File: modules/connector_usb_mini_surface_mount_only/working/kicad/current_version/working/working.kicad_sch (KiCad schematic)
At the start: 1 part, among them J1 scumnsmo

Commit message: a few module workings
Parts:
- removed J1: scumnsmo, scumnsmo_electronic_socket_usb_mini_surface_mount_only, symbol oomlout_oomp_part_symbols:scumnsmo_electronic_socket_usb_mini_surface_mount_only
- added J3: scumnsmo, oomlout_oomp_part_kicad_footprints:scumnsmo_electronic_socket_usb_mini_surface_mount_only, symbol oomlout_oomp_part_symbols:scumnsmo_electronic_socket_usb_mini_surface_mount_only
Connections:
- net +5V: now also J3.1 (VBUS)
- net GND: now also J3.5 (GND), J3.6 (Shield)
- net usb_id: now also J3.4 (ID)
- net usb_negative: now also J3.2 (D-)
- net usb_plus: now also J3.3 (D+)
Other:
- note added: "name"
- note added: "usb_mini"
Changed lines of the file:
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@@
 (kicad_sch (version 20230121) (generator eeschema)
   (paper "A4")
-  (wire (pts (xy 175.26 69.85) (xy 172.72 69.85))
+  (junction (at 142.24 109.22) (diameter 0) (color 0 0 0 0)
+  )
+  (wire (pts (xy 149.86 96.52) (xy 152.4 96.52))
     (stroke (width 0) (type default))
   )
-  (wire (pts (xy 165.1 85.09) (xy 165.1 87.63))
+  (wire (pts (xy 142.24 106.68) (xy 142.24 109.22))
     (stroke (width 0) (type default))
   )
-  (wire (pts (xy 162.56 85.09) (xy 162.56 87.63))
+  (wire (pts (xy 152.4 91.44) (xy 149.86 91.44))
     (stroke (width 0) (type default))
   )
-  (wire (pts (xy 172.72 74.93) (xy 175.26 74.93))
+  (wire (pts (xy 139.7 106.68) (xy 139.7 109.22))
     (stroke (width 0) (type default))
   )
-  (wire (pts (xy 172.72 80.01) (xy 175.26 80.01))
+  (wire (pts (xy 149.86 99.06) (xy 152.4 99.06))
     (stroke (width 0) (type default))
   )
-  (wire (pts (xy 175.26 67.31) (xy 175.26 69.85))
+  (wire (pts (xy 139.7 109.22) (xy 142.24 109.22))
     (stroke (width 0) (type default))
   )
-  (wire (pts (xy 172.72 77.47) (xy 175.26 77.47))
+  (wire (pts (xy 149.86 101.6) (xy 152.4 101.6))
     (stroke (width 0) (type default))
   )
-  (rectangle (start 137.16 40.64) (end 200.66 105.41)
+  (wire (pts (xy 152.4 88.9) (xy 152.4 91.44))
+    (stroke (width 0) (type default))
+  )
+  (rectangle (start 139.7 62.23) (end 177.8 68.58)
+    (stroke (width 1) (type default))
+    (fill (type color) (color 0 0 0 0))
+  )
+  (rectangle (start 114.3 62.23) (end 177.8 127)
     (stroke (width 1) (type default))
     (fill (type none))
   )
-  (rectangle (start 199.39 97.79) (end 199.39 97.79)
-    (stroke (width 0) (type default))
-    (fill (type none))
-  )
-  (text "module\nconnector\nusb_mini\nsurface_mount_only\n\n" (at 138.43 60.96 0)
+  (text "module\nconnector\nusb_mini\nsurface_mount_only\n\n" (at 115.57 82.55 0)
     (effects (font (size 2.5 2.5)) (justify left bottom))
   )
-  (label "usb_id" (at 175.26 80.01 0) (fields_autoplaced)
+  (text "name" (at 142.24 68.58 90)
+    (effects (font (size 1.27 1.27) (thickness 0.254) bold (color 255 255 255 1)) (justify left bottom))
+  )
+  (text "usb_mini\n" (at 176.53 68.58 0)
+    (effects (font (size 4 4) (thickness 0.8) bold (color 255 255 255 1)) (justify right bottom))
+  )
+  (label "usb_negative" (at 152.4 99.06 0) (fields_autoplaced)
     (effects (font (size 1.27 1.27)) (justify left bottom))
   )
-  (label "usb_plus" (at 175.26 74.93 0) (fields_autoplaced)
+  (label "usb_id" (at 152.4 101.6 0) (fields_autoplaced)
     (effects (font (size 1.27 1.27)) (justify left bottom))
   )
-  (label "usb_negative" (at 175.26 77.47 0) (fields_autoplaced)
+  (label "usb_plus" (at 152.4 96.52 0) (fields_autoplaced)
     (effects (font (size 1.27 1.27)) (justify left bottom))
   )
-  (label "usb_shield" (at 162.56 87.63 270) (fields_autoplaced)
-    (effects (font (size 1.27 1.27)) (justify right bottom))
-  )
-  (symbol (lib_id "oomlout_oomp_part_symbols:scumnsmo_electronic_socket_usb_mini_surface_mount_only") (at 165.1 74.93 0) (unit 1)
+  (symbol (lib_id "power:+5V") (at 152.4 88.9 0) (unit 1)
     (in_bom yes) (on_board yes) (dnp no) (fields_autoplaced)
-    (property "Reference" "J1" (at 165.1 62.23 0)
+    (property "Reference" "#PWR013" (at 152.4 92.71 0)
+      (effects (font (size 1.27 1.27)) hide)
+    )
+    (property "Value" "+5V" (at 152.4 83.82 0)
       (effects (font (size 1.27 1.27)))
     )
-    (property "Value" "scumnsmo" (at 165.1 64.77 0)
+    (property "Footprint" "" (at 152.4 88.9 0)
+      (effects (font (size 1.27 1.27)) hide)
+    )
+    (property "Datasheet" "" (at 152.4 88.9 0)
+      (effects (font (size 1.27 1.27)) hide)
+    )
+    (pin "1")
+    (instances
+      (project "working"
+        (path "/5407c114-4107-4d84-8382-1717fb9d687c"
+          (reference "#PWR013") (unit 1)
+        )
+      )
+      (project "working"
+        (path "/d7ac9d55-1973-40f4-b2a5-38a433b49fa0"
+          (reference "#PWR02") (unit 1)
+        )
+      )
+    )
+  )
+  (symbol (lib_id "oomlout_oomp_part_symbols:scumnsmo_electronic_socket_usb_mini_surface_mount_only") (at 142.24 96.52 0) (unit 1)
+    (in_bom yes) (on_board yes) (dnp no) (fields_autoplaced)
+    (property "Reference" "J3" (at 142.24 83.82 0)
       (effects (font (size 1.27 1.27)))
     )
-    (property "Footprint" "scumnsmo_electronic_socket_usb_mini_surface_mount_only" (at 168.91 76.2 0)
+    (property "Value" "scumnsmo" (at 142.24 86.36 0)
+      (effects (font (size 1.27 1.27)))
+    )
+    (property "Footprint" "oomlout_oomp_part_kicad_footprints:scumnsmo_electronic_socket_usb_mini_surface_mount_only" (at 146.05 97.79 0)
       (effects (font (size 1.27 1.27)) hide)
     )
-    (property "Datasheet" "https://github.com/oomlout/oomlout_oomp_v3/parts/electronic_socket_usb_mini_surface_mount_only/datasheet.pdf" (at 168.91 76.2 0)
+    (property "Datasheet" "https://github.com/oomlout/oomlout_oomp_v3/parts/electronic_socket_usb_mini_surface_mount_only/datasheet.pdf" (at 146.05 97.79 0)
       (effects (font (size 1.27 1.27)) hide)
     )
@@
     (instances
       (project "working"
+        (path "/5407c114-4107-4d84-8382-1717fb9d687c"
+          (reference "J3") (unit 1)
+        )
+      )
+      (project "working"
         (path "/d7ac9d55-1973-40f4-b2a5-38a433b49fa0"
           (reference "J1") (unit 1)
@@
     )
   )
-  (symbol (lib_id "power:+5V") (at 175.26 67.31 0) (unit 1)
+  (symbol (lib_id "power:GND") (at 142.24 109.22 0) (unit 1)
     (in_bom yes) (on_board yes) (dnp no) (fields_autoplaced)
-    (property "Reference" "#PWR04" (at 175.26 71.12 0)
+    (property "Reference" "#PWR012" (at 142.24 115.57 0)
       (effects (font (size 1.27 1.27)) hide)
     )
-    (property "Value" "+5V" (at 175.26 62.23 0)
+    (property "Value" "GND" (at 142.24 114.3 0)
       (effects (font (size 1.27 1.27)))
     )
-    (property "Footprint" "" (at 175.26 67.31 0)
+    (property "Footprint" "" (at 142.24 109.22 0)
       (effects (font (size 1.27 1.27)) hide)
     )
-    (property "Datasheet" "" (at 175.26 67.31 0)
+    (property "Datasheet" "" (at 142.24 109.22 0)
       (effects (font (size 1.27 1.27)) hide)
     )
@@
     (instances
       (project "working"
-        (path "/d7ac9d55-1973-40f4-b2a5-38a433b49fa0"
-          (reference "#PWR04") (unit 1)
+        (path "/5407c114-4107-4d84-8382-1717fb9d687c"
+          (reference "#PWR012") (unit 1)
         )
       )
-    )
-  )
-  (symbol (lib_id "power:GND") (at 165.1 87.63 0) (unit 1)
-    (in_bom yes) (on_board yes) (dnp no) (fields_autoplaced)
-    (property "Reference" "#PWR03" (at 165.1 93.98 0)
-      (effects (font (size 1.27 1.27)) hide)
-    )
-    (property "Value" "GND" (at 165.1 92.71 0)
-      (effects (font (size 1.27 1.27)))
-    )
-    (property "Footprint" "" (at 165.1 87.63 0)
-      (effects (font (size 1.27 1.27)) hide)
-    )
-    (property "Datasheet" "" (at 165.1 87.63 0)
-      (effects (font (size 1.27 1.27)) hide)
-    )
-    (pin "1")
-    (instances
       (project "working"
         (path "/d7ac9d55-1973-40f4-b2a5-38a433b49fa0"
-          (reference "#PWR03") (unit 1)
+          (reference "#PWR01") (unit 1)
         )
       )

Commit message: works.
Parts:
- removed J3: scumnsmo, oomlout_oomp_part_kicad_footprints:scumnsmo_electronic_socket_usb_mini_surface_mount_only, symbol oomlout_oomp_part_symbols:scumnsmo_electronic_socket_usb_mini_surface_mount_only
- added J1: scumnsmo, oomlout_oomp_part_footprints:scumnsmo_electronic_socket_usb_mini_surface_mount_only, symbol oomlout_oomp_part_symbols:scumnsmo_electronic_socket_usb_mini_surface_mount_only
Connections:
- net +5V: now also J1.1 (VBUS)
- net GND: now also J1.5 (GND), J1.6 (Shield)
- net usb_id: now also J1.4 (ID)
- net usb_negative: now also J1.2 (D-)
- new net usb_positive: J1.3 (D+)
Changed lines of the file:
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@@
 (kicad_sch (version 20230121) (generator eeschema)
   (paper "A4")
-  (junction (at 142.24 109.22) (diameter 0) (color 0 0 0 0)
+  (junction (at 146.05 110.49) (diameter 0) (color 0 0 0 0)
   )
-  (wire (pts (xy 149.86 96.52) (xy 152.4 96.52))
+  (wire (pts (xy 153.67 102.87) (xy 156.21 102.87))
     (stroke (width 0) (type default))
   )
-  (wire (pts (xy 142.24 106.68) (xy 142.24 109.22))
+  (wire (pts (xy 146.05 107.95) (xy 146.05 110.49))
     (stroke (width 0) (type default))
   )
-  (wire (pts (xy 152.4 91.44) (xy 149.86 91.44))
+  (wire (pts (xy 156.21 90.17) (xy 156.21 92.71))
     (stroke (width 0) (type default))
   )
-  (wire (pts (xy 139.7 106.68) (xy 139.7 109.22))
+  (wire (pts (xy 153.67 97.79) (xy 156.21 97.79))
     (stroke (width 0) (type default))
   )
-  (wire (pts (xy 149.86 99.06) (xy 152.4 99.06))
+  (wire (pts (xy 143.51 110.49) (xy 146.05 110.49))
     (stroke (width 0) (type default))
   )
-  (wire (pts (xy 139.7 109.22) (xy 142.24 109.22))
+  (wire (pts (xy 153.67 92.71) (xy 156.21 92.71))
     (stroke (width 0) (type default))
   )
-  (wire (pts (xy 149.86 101.6) (xy 152.4 101.6))
+  (wire (pts (xy 143.51 107.95) (xy 143.51 110.49))
     (stroke (width 0) (type default))
   )
-  (wire (pts (xy 152.4 88.9) (xy 152.4 91.44))
+  (wire (pts (xy 153.67 100.33) (xy 156.21 100.33))
     (stroke (width 0) (type default))
   )
-  (rectangle (start 139.7 62.23) (end 177.8 68.58)
+  (rectangle (start 118.11 60.96) (end 181.61 125.73)
+    (stroke (width 1) (type default))
+    (fill (type none))
+  )
+  (rectangle (start 143.51 60.96) (end 181.61 67.31)
     (stroke (width 1) (type default))
     (fill (type color) (color 0 0 0 0))
   )
-  (rectangle (start 114.3 62.23) (end 177.8 127)
-    (stroke (width 1) (type default))
-    (fill (type none))
+  (text "usb_mini" (at 181.61 66.04 0)
+    (effects (font (size 3 3) (thickness 0.8) bold (color 255 255 255 1)) (justify right bottom))
   )
-  (text "module\nconnector\nusb_mini\nsurface_mount_only\n\n" (at 115.57 82.55 0)
+  (text "name" (at 146.05 67.31 90)
+    (effects (font (size 1.27 1.27) (thickness 0.254) bold (color 255 255 255 1)) (justify left bottom))
+  )
+  (text "module\nconnector\nusb_mini\nsurface_mount_only\n\n" (at 119.38 81.28 0)
     (effects (font (size 2.5 2.5)) (justify left bottom))
   )
-  (text "name" (at 142.24 68.58 90)
-    (effects (font (size 1.27 1.27) (thickness 0.254) bold (color 255 255 255 1)) (justify left bottom))
-  )
-  (text "usb_mini\n" (at 176.53 68.58 0)
-    (effects (font (size 4 4) (thickness 0.8) bold (color 255 255 255 1)) (justify right bottom))
-  )
-  (label "usb_negative" (at 152.4 99.06 0) (fields_autoplaced)
+  (label "usb_id" (at 156.21 102.87 0) (fields_autoplaced)
     (effects (font (size 1.27 1.27)) (justify left bottom))
   )
-  (label "usb_id" (at 152.4 101.6 0) (fields_autoplaced)
+  (label "usb_positive" (at 156.21 97.79 0) (fields_autoplaced)
     (effects (font (size 1.27 1.27)) (justify left bottom))
   )
-  (label "usb_plus" (at 152.4 96.52 0) (fields_autoplaced)
+  (label "usb_negative" (at 156.21 100.33 0) (fields_autoplaced)
     (effects (font (size 1.27 1.27)) (justify left bottom))
   )
-  (symbol (lib_id "power:+5V") (at 152.4 88.9 0) (unit 1)
+  (symbol (lib_id "power:GND") (at 146.05 110.49 0) (unit 1)
     (in_bom yes) (on_board yes) (dnp no) (fields_autoplaced)
-    (property "Reference" "#PWR013" (at 152.4 92.71 0)
+    (property "Reference" "#PWR012" (at 146.05 116.84 0)
       (effects (font (size 1.27 1.27)) hide)
     )
-    (property "Value" "+5V" (at 152.4 83.82 0)
+    (property "Value" "GND" (at 146.05 115.57 0)
       (effects (font (size 1.27 1.27)))
     )
-    (property "Footprint" "" (at 152.4 88.9 0)
+    (property "Footprint" "" (at 146.05 110.49 0)
       (effects (font (size 1.27 1.27)) hide)
     )
-    (property "Datasheet" "" (at 152.4 88.9 0)
+    (property "Datasheet" "" (at 146.05 110.49 0)
+      (effects (font (size 1.27 1.27)) hide)
+    )
+    (pin "1")
+    (instances
+      (project "working"
+        (path "/5407c114-4107-4d84-8382-1717fb9d687c"
+          (reference "#PWR012") (unit 1)
+        )
+      )
+      (project "working"
+        (path "/d7ac9d55-1973-40f4-b2a5-38a433b49fa0"
+          (reference "#PWR01") (unit 1)
+        )
+      )
+    )
+  )
+  (symbol (lib_id "power:+5V") (at 156.21 90.17 0) (unit 1)
+    (in_bom yes) (on_board yes) (dnp no) (fields_autoplaced)
+    (property "Reference" "#PWR013" (at 156.21 93.98 0)
+      (effects (font (size 1.27 1.27)) hide)
+    )
+    (property "Value" "+5V" (at 156.21 85.09 0)
+      (effects (font (size 1.27 1.27)))
+    )
+    (property "Footprint" "" (at 156.21 90.17 0)
+      (effects (font (size 1.27 1.27)) hide)
+    )
+    (property "Datasheet" "" (at 156.21 90.17 0)
       (effects (font (size 1.27 1.27)) hide)
     )
@@
     )
   )
-  (symbol (lib_id "oomlout_oomp_part_symbols:scumnsmo_electronic_socket_usb_mini_surface_mount_only") (at 142.24 96.52 0) (unit 1)
+  (symbol (lib_id "oomlout_oomp_part_symbols:scumnsmo_electronic_socket_usb_mini_surface_mount_only") (at 146.05 97.79 0) (unit 1)
     (in_bom yes) (on_board yes) (dnp no) (fields_autoplaced)
-    (property "Reference" "J3" (at 142.24 83.82 0)
+    (property "Reference" "J1" (at 146.05 85.09 0)
       (effects (font (size 1.27 1.27)))
     )
-    (property "Value" "scumnsmo" (at 142.24 86.36 0)
+    (property "Value" "scumnsmo" (at 146.05 87.63 0)
       (effects (font (size 1.27 1.27)))
     )
-    (property "Footprint" "oomlout_oomp_part_kicad_footprints:scumnsmo_electronic_socket_usb_mini_surface_mount_only" (at 146.05 97.79 0)
+    (property "Footprint" "oomlout_oomp_part_footprints:scumnsmo_electronic_socket_usb_mini_surface_mount_only" (at 149.86 99.06 0)
       (effects (font (size 1.27 1.27)) hide)
     )
-    (property "Datasheet" "https://github.com/oomlout/oomlout_oomp_v3/parts/electronic_socket_usb_mini_surface_mount_only/datasheet.pdf" (at 146.05 97.79 0)
+    (property "Datasheet" "https://github.com/oomlout/oomlout_oomp_v3/parts/electronic_socket_usb_mini_surface_mount_only/datasheet.pdf" (at 149.86 99.06 0)
       (effects (font (size 1.27 1.27)) hide)
     )
@@
     (instances
       (project "working"
-        (path "/5407c114-4107-4d84-8382-1717fb9d687c"
-          (reference "J3") (unit 1)
-        )
-      )
-      (project "working"
         (path "/d7ac9d55-1973-40f4-b2a5-38a433b49fa0"
           (reference "J1") (unit 1)
         )
       )
-    )
-  )
-  (symbol (lib_id "power:GND") (at 142.24 109.22 0) (unit 1)
-    (in_bom yes) (on_board yes) (dnp no) (fields_autoplaced)
-    (property "Reference" "#PWR012" (at 142.24 115.57 0)
-      (effects (font (size 1.27 1.27)) hide)
-    )
-    (property "Value" "GND" (at 142.24 114.3 0)
-      (effects (font (size 1.27 1.27)))
-    )
-    (property "Footprint" "" (at 142.24 109.22 0)
-      (effects (font (size 1.27 1.27)) hide)
-    )
-    (property "Datasheet" "" (at 142.24 109.22 0)
-      (effects (font (size 1.27 1.27)) hide)
-    )
-    (pin "1")
-    (instances
-      (project "working"
-        (path "/5407c114-4107-4d84-8382-1717fb9d687c"
-          (reference "#PWR012") (unit 1)
-        )
-      )
-      (project "working"
-        (path "/d7ac9d55-1973-40f4-b2a5-38a433b49fa0"
-          (reference "#PWR01") (unit 1)
-        )
-      )

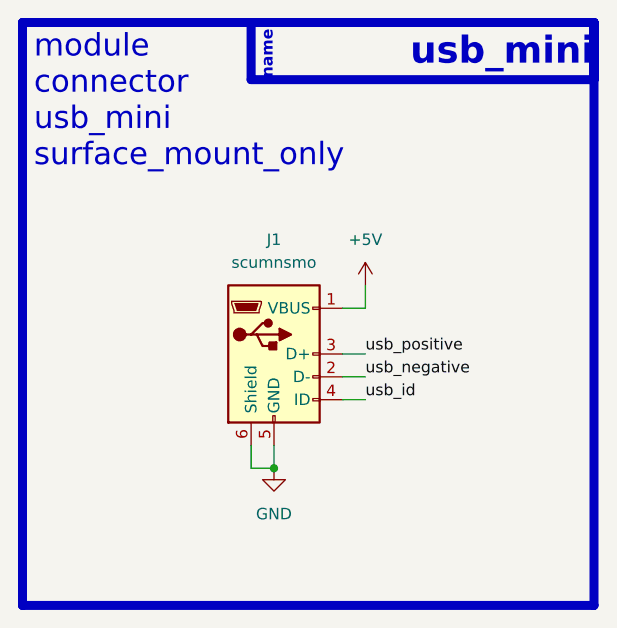
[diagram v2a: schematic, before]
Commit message: fixed formatting to be more consistent
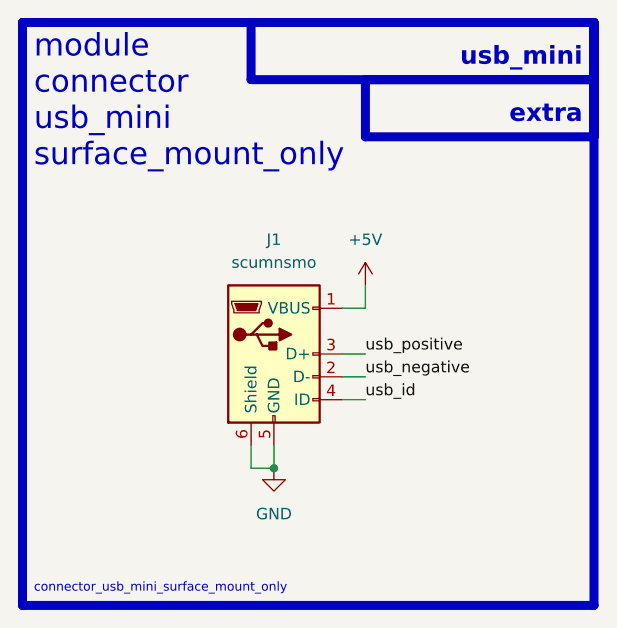
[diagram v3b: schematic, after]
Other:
- note added: "connector_usb_mini_surface_mount_only"
- note added: "extra"
- note removed: "name"
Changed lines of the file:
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@@
+    (fill (type none))
+  )
+  (rectangle (start 156.21 67.31) (end 181.61 73.66)
+    (stroke (width 1) (type default))
     (fill (type none))
   )
   (rectangle (start 143.51 60.96) (end 181.61 67.31)
     (stroke (width 1) (type default))
-    (fill (type color) (color 0 0 0 0))
+    (fill (type none))
   )
-  (text "usb_mini" (at 181.61 66.04 0)
-    (effects (font (size 3 3) (thickness 0.8) bold (color 255 255 255 1)) (justify right bottom))
+  (text "extra" (at 180.34 72.39 0)
+    (effects (font (size 2 2) (thickness 0.8) bold) (justify right bottom))
   )
-  (text "name" (at 146.05 67.31 90)
-    (effects (font (size 1.27 1.27) (thickness 0.254) bold (color 255 255 255 1)) (justify left bottom))
+  (text "usb_mini" (at 180.34 66.04 0)
+    (effects (font (size 2 2) (thickness 0.8) bold) (justify right bottom))
   )
   (text "module\nconnector\nusb_mini\nsurface_mount_only\n\n" (at 119.38 81.28 0)
     (effects (font (size 2.5 2.5)) (justify left bottom))
   )
+  (text "connector_usb_mini_surface_mount_only" (at 119.38 124.46 0)
+    (effects (font (size 1 1)) (justify left bottom))
+  )
   (label "usb_id" (at 156.21 102.87 0) (fields_autoplaced)
